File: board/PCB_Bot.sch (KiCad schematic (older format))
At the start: 19 parts, among them J1 Screw_Terminal_01x04, J2 Conn_02x15_Top_Bottom, J3 Conn_02x15_Top_Bottom, J4 Screw_Terminal_01x02, J5 Conn_02x03_Top_Bottom, U1 TB6612FNG, U2 LSM9DS1

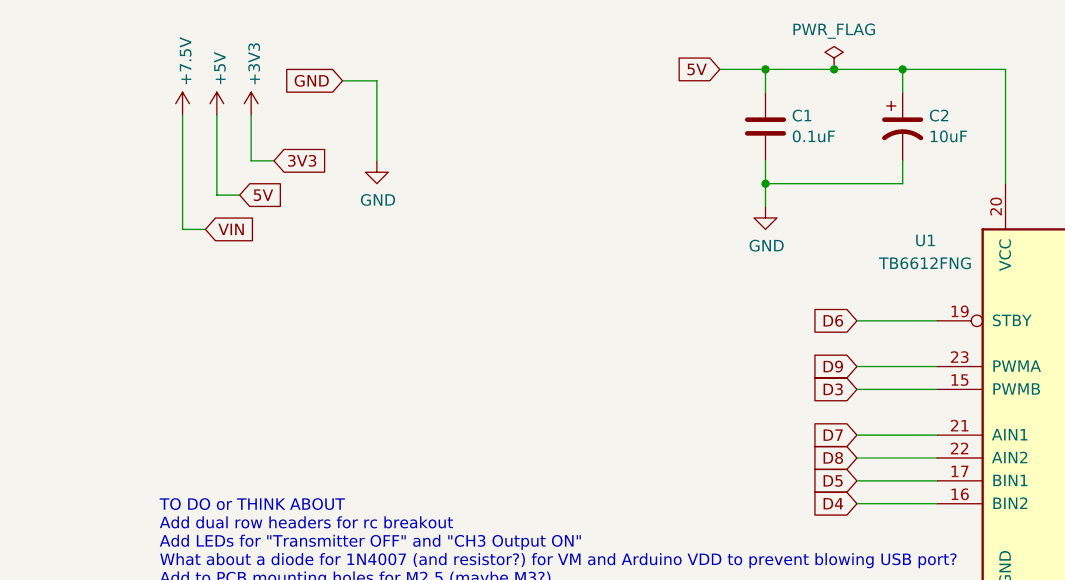
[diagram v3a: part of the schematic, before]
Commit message: update power flags in schematic, check erros and warnings - all warnings now
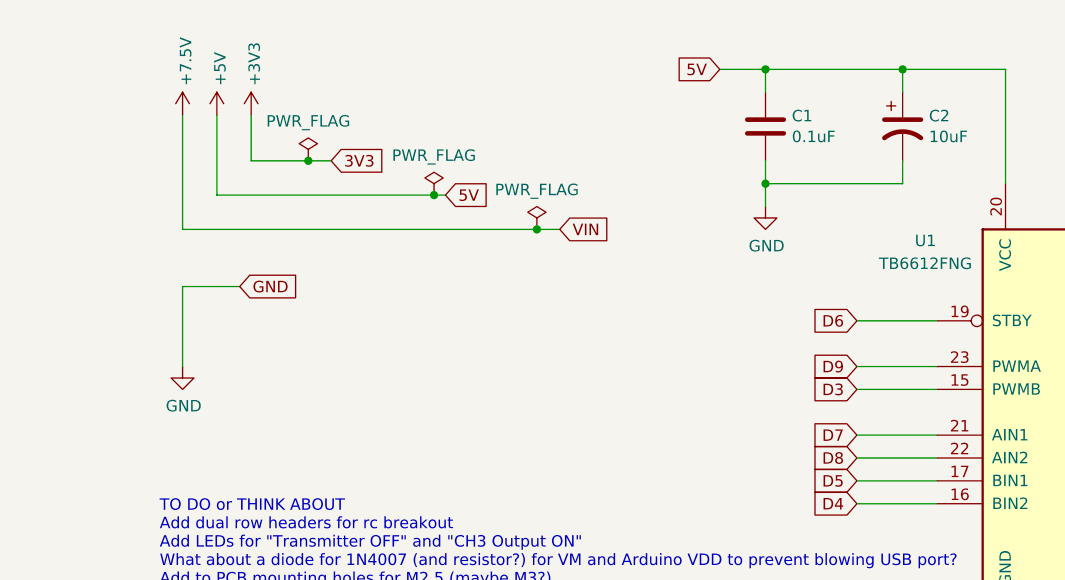
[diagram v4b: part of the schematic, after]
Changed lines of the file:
@@
 	1    0    0    -1
 $EndComp
-Text GLabel 1000 1300 2    50   Input ~ 0
+Text GLabel 1900 1300 2    50   Input ~ 0
 5V
-Text GLabel 1150 1150 2    50   Input ~ 0
+Text GLabel 1400 1150 2    50   Input ~ 0
 3V3
 Text Notes 650  3900 0    50   ~ 0
@@
 	1    0    0    -1
 $EndComp
-Text GLabel 850  1450 2    50   Input ~ 0
+Text GLabel 2400 1450 2    50   Input ~ 0
 VIN
 Text GLabel 3100 750  0    50   Input ~ 0
@@
 Wire Wire Line
 	4950 750  5250 750
-Text GLabel 1450 800  0    50   Input ~ 0
+Text GLabel 1000 1700 2    50   Input ~ 0
 GND
 Wire Wire Line
-	1450 800  1600 800
-Wire Wire Line
-	1600 800  1600 1150
+	750  1700 750  2050
 Wire Wire Line
 	3700 1850 4050 1850
@@
 Connection ~ 3300 750
 Wire Wire Line
-	3300 750  3600 750
-Wire Wire Line
 	3300 1150 3300 1250
 Wire Wire Line
@@
 	750  950  750  1450
 Wire Wire Line
-	750  1450 850  1450
+	750  1450 2300 1450
 Wire Wire Line
 	900  950  900  1300
 Wire Wire Line
-	900  1300 1000 1300
+	900  1300 1850 1300
 Wire Wire Line
 	1050 950  1050 1150
 Wire Wire Line
-	1050 1150 1150 1150
+	1050 1150 1300 1150
 $Comp
 L power:GND #PWR04
 U 1 1 5E51BDF2
-P 1600 1150
-F 0 "#PWR04" H 1600 900 50  0001 C CNN
-F 1 "GND" H 1605 977 50  0000 C CNN
-F 2 "" H 1600 1150 50  0001 C CNN
-F 3 "" H 1600 1150 50  0001 C CNN
-	1    1600 1150
+P 750 2050
+F 0 "#PWR04" H 750 1800 50  0001 C CNN
+F 1 "GND" H 755 1877 50  0000 C CNN
+F 2 "" H 750 2050 50  0001 C CNN
+F 3 "" H 750 2050 50  0001 C CNN
+	1    750  2050
 	1    0    0    -1
 $EndComp
@@
 Text GLabel 7250 3100 2    50   Input ~ 0
 D12
-$Comp
-L power:PWR_FLAG #FLG0101
-U 1 1 5E56B89A
-P 3600 750
-F 0 "#FLG0101" H 3600 825 50  0001 C CNN
-F 1 "PWR_FLAG" H 3600 923 50  0000 C CNN
-F 2 "" H 3600 750 50  0001 C CNN
-F 3 "~" H 3600 750 50  0001 C CNN
-	1    3600 750
-	1    0    0    -1
-$EndComp
-Connection ~ 3600 750
-Wire Wire Line
-	3600 750  3900 750
 Text GLabel 6300 2900 0    50   Input ~ 0
 GND
@@
 Wire Wire Line
 	6500 3100 6300 3100
+Wire Wire Line
+	3300 750  3900 750
+$Comp
+L power:PWR_FLAG #FLG0101
+U 1 1 5E5FEFE6
+P 1300 1150
+F 0 "#FLG0101" H 1300 1225 50  0001 C CNN
+F 1 "PWR_FLAG" H 1300 1323 50  0000 C CNN
+F 2 "" H 1300 1150 50  0001 C CNN
+F 3 "~" H 1300 1150 50  0001 C CNN
+	1    1300 1150
+	1    0    0    -1
+$EndComp
+Connection ~ 1300 1150
+Wire Wire Line
+	1300 1150 1400 1150
+$Comp
+L power:PWR_FLAG #FLG0102
+U 1 1 5E5FF70B
+P 1850 1300
+F 0 "#FLG0102" H 1850 1375 50  0001 C CNN
+F 1 "PWR_FLAG" H 1850 1473 50  0000 C CNN
+F 2 "" H 1850 1300 50  0001 C CNN
+F 3 "~" H 1850 1300 50  0001 C CNN
+	1    1850 1300
+	1    0    0    -1
+$EndComp
+Connection ~ 1850 1300
+Wire Wire Line
+	1850 1300 1900 1300
+$Comp
+L power:PWR_FLAG #FLG0103
+U 1 1 5E5FFA8B
+P 2300 1450
+F 0 "#FLG0103" H 2300 1525 50  0001 C CNN
+F 1 "PWR_FLAG" H 2300 1623 50  0000 C CNN
+F 2 "" H 2300 1450 50  0001 C CNN
+F 3 "~" H 2300 1450 50  0001 C CNN
+	1    2300 1450
+	1    0    0    -1
+$EndComp
+Connection ~ 2300 1450
+Wire Wire Line
+	2300 1450 2400 1450
+Wire Wire Line
+	750  1700 1000 1700
 $EndSCHEMATC
